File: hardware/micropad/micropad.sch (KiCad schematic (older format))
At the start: 24 parts, among them J1 OLED Connector, J2 Conn_ARM_JTAG_SWD_10, J3 USB_B_Micro, SW1 SW_SPST, SW2 SW_SPST, SW3 SW_SPST, U1 LD1117S33TR_SOT223, U2 STM32F042K6Ux

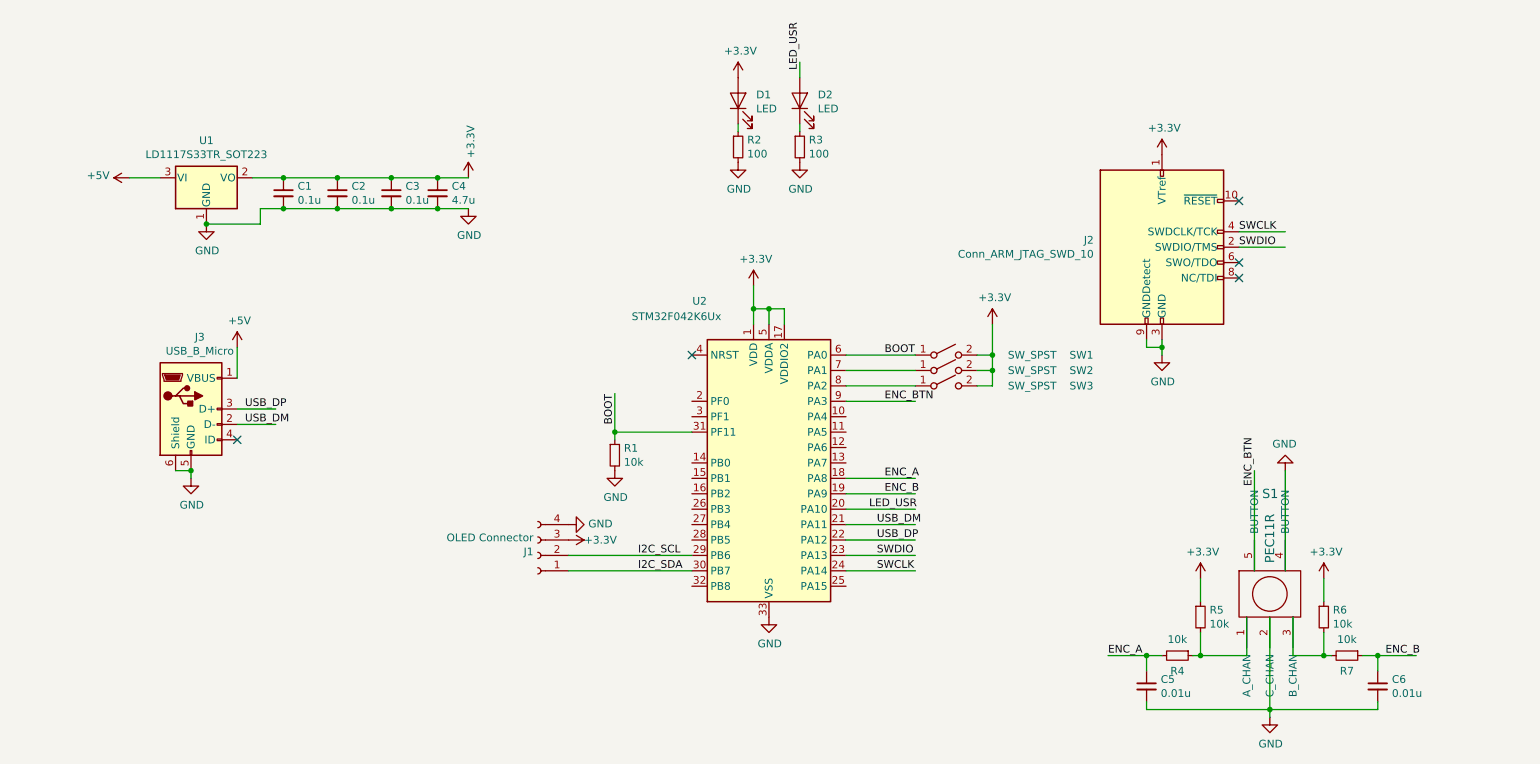
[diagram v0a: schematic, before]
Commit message: Swap in an APA102 instead of the OLED screen
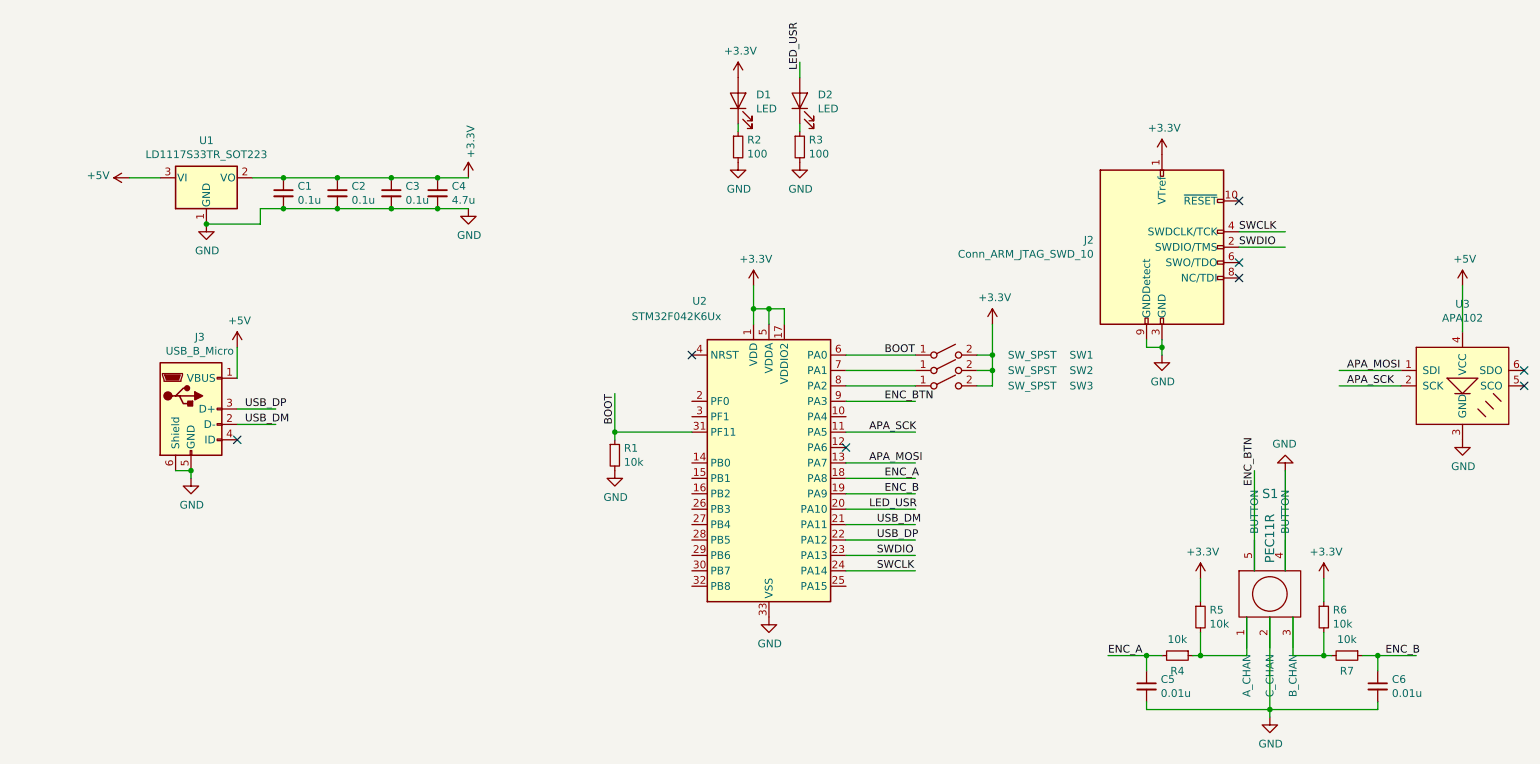
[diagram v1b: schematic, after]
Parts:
- removed J1: OLED Connector, Pin_Headers:Pin_Header_Straight_1x04_Pitch2.54mm, symbol Connector:Conn_01x04_Female
- added U3: APA102, LEDs:LED_RGB_5050-6, symbol apa102:APA102
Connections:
- net labels added: APA_MOSI, APA_SCK
- net labels removed: I2C_SCL, I2C_SDA
- wire segments 79 -> 82
- no-connect marks 5 -> 8
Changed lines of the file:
@@
 Text Label 6350 4550 0    50   ~ 0
 USB_DP
-Text Label 4800 4650 0    50   ~ 0
-I2C_SCL
-Text Label 4800 4750 0    50   ~ 0
-I2C_SDA
 Wire Wire Line
 	2200 3800 2450 3800
@@
 	6150 3550 6600 3550
 $Comp
-L power:+3.3V #PWR08
-U 1 1 5FAF7B5A
-P 4350 4550
-F 0 "#PWR08" H 4350 4400 50  0001 C CNN
-F 1 "+3.3V" V 4350 4650 50  0000 L CNN
-F 2 "" H 4350 4550 50  0001 C CNN
-F 3 "" H 4350 4550 50  0001 C CNN
-	1    4350 4550
-	0    1    1    0
-$EndComp
-$Comp
-L power:GND #PWR07
-U 1 1 5FAF7679
-P 4350 4450
-F 0 "#PWR07" H 4350 4200 50  0001 C CNN
-F 1 "GND" V 4355 4322 50  0000 R CNN
-F 2 "" H 4350 4450 50  0001 C CNN
-F 3 "" H 4350 4450 50  0001 C CNN
-	1    4350 4450
-	0    -1   -1   0
-$EndComp
-$Comp
-L Connector:Conn_01x04_Female J1
-U 1 1 5FAEAC8B
-P 4150 4650
-F 0 "J1" H 4178 4626 50  0000 L CNN
-F 1 "OLED Connector" H 4178 4535 50  0000 L CNN
-F 2 "Pin_Headers:Pin_Header_Straight_1x04_Pitch2.54mm" H 4150 4650 50  0001 C CNN
-F 3 "~" H 4150 4650 50  0001 C CNN
-	1    4150 4650
-	-1   0    0    1
-$EndComp
-Wire Wire Line
-	4350 4650 5150 4650
-Wire Wire Line
-	4350 4750 5150 4750
-$Comp
 L Switch:SW_SPST SW1
 U 1 1 5FAE673E
@@
 Connection ~ 1900 4100
 NoConn ~ 2200 3900
+$Comp
+L apa102:APA102 U3
+U 1 1 5FB655DF
+P 10150 3550
+F 0 "U3" H 10150 4081 50  0000 C CNN
+F 1 "APA102" H 10150 3990 50  0000 C CNN
+F 2 "LEDs:LED_RGB_5050-6" H 10150 3550 50  0001 C CNN
+F 3 "" H 10150 3550 50  0001 C CNN
+	1    10150 3550
+	1    0    0    -1
+$EndComp
+Text Label 9400 3550 0    50   ~ 0
+APA_SCK
+Text Label 9400 3450 0    50   ~ 0
+APA_MOSI
+Wire Wire Line
+	9350 3550 9750 3550
+Wire Wire Line
+	9350 3450 9750 3450
+Wire Wire Line
+	10150 3200 10150 2900
+$Comp
+L power:+5V #PWR07
+U 1 1 5FB8AF8D
+P 10150 2900
+F 0 "#PWR07" H 10150 2750 50  0001 C CNN
+F 1 "+5V" H 10165 3073 50  0000 C CNN
+F 2 "" H 10150 2900 50  0001 C CNN
+F 3 "" H 10150 2900 50  0001 C CNN
+	1    10150 2900
+	1    0    0    -1
+$EndComp
+$Comp
+L power:GND #PWR08
+U 1 1 5FB8B6CE
+P 10150 3900
+F 0 "#PWR08" H 10150 3650 50  0001 C CNN
+F 1 "GND" H 10155 3727 50  0000 C CNN
+F 2 "" H 10150 3900 50  0001 C CNN
+F 3 "" H 10150 3900 50  0001 C CNN
+	1    10150 3900
+	1    0    0    -1
+$EndComp
+NoConn ~ 10550 3450
+NoConn ~ 10550 3550
+Wire Wire Line
+	6150 3850 6600 3850
+Text Label 6300 3850 0    50   ~ 0
+APA_SCK
+Wire Wire Line
+	6150 4050 6600 4050
+Text Label 6300 4050 0    50   ~ 0
+APA_MOSI
+NoConn ~ 6150 3950
 $EndSCHEMATC

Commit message: Use a QFN32 package that's easier to work with
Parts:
- U2: footprint Housings_DFN_QFN:WQFN-32-1EP_5x5mm_Pitch0.5mm -> Housings_DFN_QFN:QFN-32-1EP_5x5mm_Pitch0.5mm
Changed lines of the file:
@@
 F 0 "U2" H 5200 5100 50  0000 C CNN
 F 1 "STM32F042K6Ux" H 5050 5000 50  0000 C CNN
-F 2 "Housings_DFN_QFN:WQFN-32-1EP_5x5mm_Pitch0.5mm" H 5250 3150 50  0001 R CNN
+F 2 "Housings_DFN_QFN:QFN-32-1EP_5x5mm_Pitch0.5mm" H 5250 3150 50  0001 R CNN
 F 3 "http://www.st.com/st-web-ui/static/active/en/resource/technical/document/datasheet/DM00105814.pdf" H 5650 4050 50  0001 C CNN
 	1    5650 4050

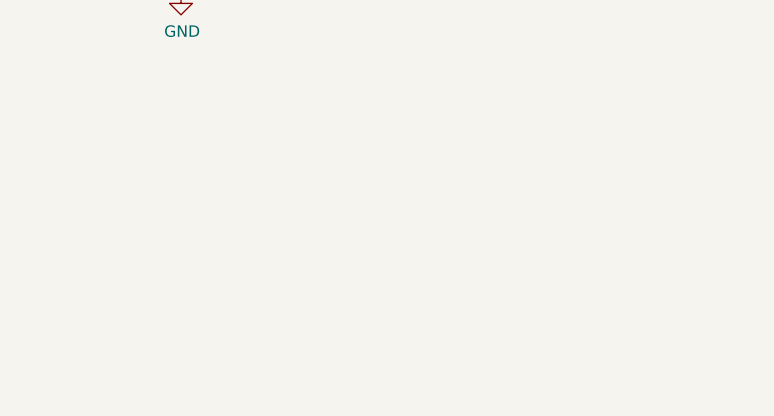
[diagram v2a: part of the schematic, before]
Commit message: Add mounting holes
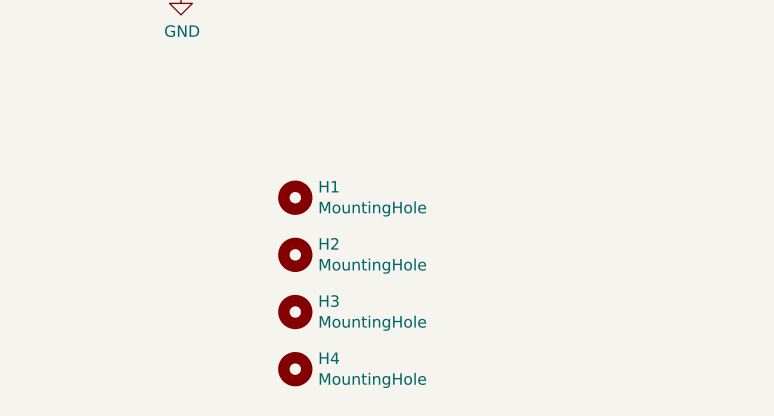
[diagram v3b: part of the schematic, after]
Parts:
- added H1, H2, H3, H4: MountingHole, Mounting_Holes:MountingHole_2.2mm_M2, symbol Mechanical:MountingHole
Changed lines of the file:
@@
 APA_MOSI
 NoConn ~ 6150 3950
+$Comp
+L Mechanical:MountingHole H1
+U 1 1 5FB65D0A
+P 2400 5050
+F 0 "H1" H 2500 5096 50  0000 L CNN
+F 1 "MountingHole" H 2500 5005 50  0000 L CNN
+F 2 "Mounting_Holes:MountingHole_2.2mm_M2" H 2400 5050 50  0001 C CNN
+F 3 "~" H 2400 5050 50  0001 C CNN
+	1    2400 5050
+	1    0    0    -1
+$EndComp
+$Comp
+L Mechanical:MountingHole H2
+U 1 1 5FB66F3B
+P 2400 5300
+F 0 "H2" H 2500 5346 50  0000 L CNN
+F 1 "MountingHole" H 2500 5255 50  0000 L CNN
+F 2 "Mounting_Holes:MountingHole_2.2mm_M2" H 2400 5300 50  0001 C CNN
+F 3 "~" H 2400 5300 50  0001 C CNN
+	1    2400 5300
+	1    0    0    -1
+$EndComp
+$Comp
+L Mechanical:MountingHole H3
+U 1 1 5FB67520
+P 2400 5550
+F 0 "H3" H 2500 5596 50  0000 L CNN
+F 1 "MountingHole" H 2500 5505 50  0000 L CNN
+F 2 "Mounting_Holes:MountingHole_2.2mm_M2" H 2400 5550 50  0001 C CNN
+F 3 "~" H 2400 5550 50  0001 C CNN
+	1    2400 5550
+	1    0    0    -1
+$EndComp
+$Comp
+L Mechanical:MountingHole H4
+U 1 1 5FB67D38
+P 2400 5800
+F 0 "H4" H 2500 5846 50  0000 L CNN
+F 1 "MountingHole" H 2500 5755 50  0000 L CNN
+F 2 "Mounting_Holes:MountingHole_2.2mm_M2" H 2400 5800 50  0001 C CNN
+F 3 "~" H 2400 5800 50  0001 C CNN
+	1    2400 5800
+	1    0    0    -1
+$EndComp
 $EndSCHEMATC

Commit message: Route remaining tracks
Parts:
- U1: footprint TO_SOT_Packages_SMD:SOT-223-3_TabPin2 -> TO_SOT_Packages_SMD:SOT-223
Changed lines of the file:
@@
 F 0 "U1" H 2000 2442 50  0000 C CNN
 F 1 "LD1117S33TR_SOT223" H 2000 2351 50  0000 C CNN
-F 2 "TO_SOT_Packages_SMD:SOT-223-3_TabPin2" H 2000 2400 50  0001 C CNN
+F 2 "TO_SOT_Packages_SMD:SOT-223" H 2000 2400 50  0001 C CNN
 F 3 "http://www.st.com/st-web-ui/static/active/en/resource/technical/document/datasheet/CD00000544.pdf" H 2100 1950 50  0001 C CNN
 	1    2000 2200

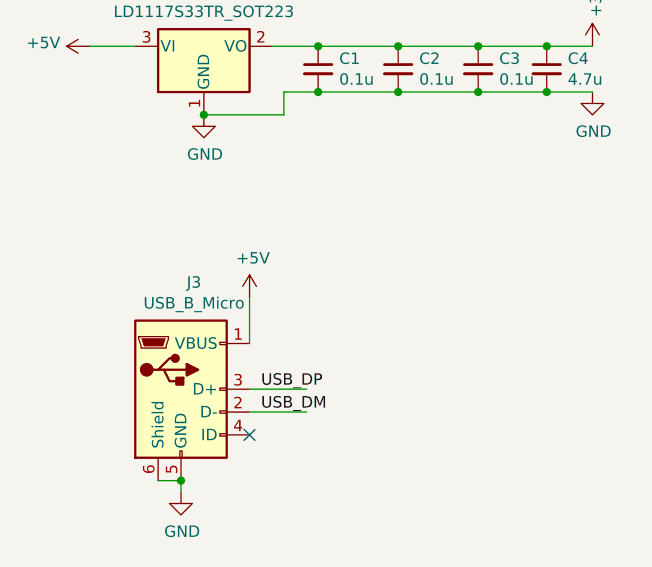
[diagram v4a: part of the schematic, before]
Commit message: Add fuse, fixup DRC and labels
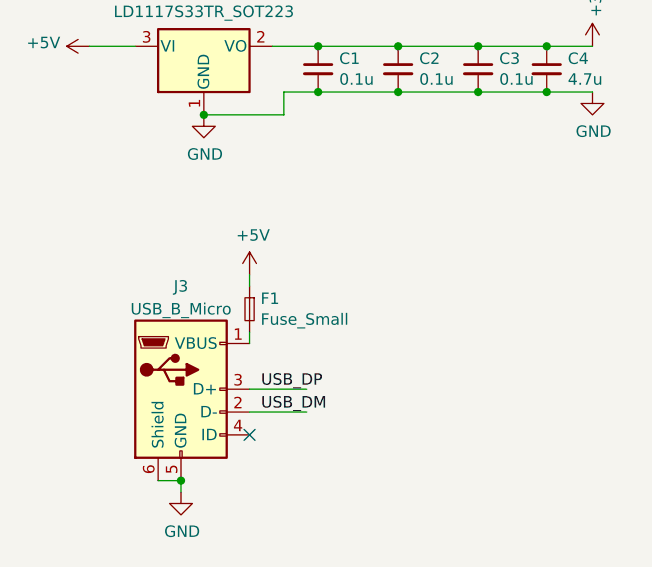
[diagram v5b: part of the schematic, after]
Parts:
- added F1: Fuse_Small, Capacitors_SMD:C_0603, symbol Device:Fuse_Small
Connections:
- wire segments 82 -> 83
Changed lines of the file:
@@
 	1    0    0    -1
 $EndComp
-Wire Wire Line
-	2200 3500 2200 3300
 $Comp
 L power:+5V #PWR04
 U 1 1 5FB029A9
-P 2200 3300
-F 0 "#PWR04" H 2200 3150 50  0001 C CNN
-F 1 "+5V" H 2215 3473 50  0000 C CNN
-F 2 "" H 2200 3300 50  0001 C CNN
-F 3 "" H 2200 3300 50  0001 C CNN
-	1    2200 3300
+P 2200 3200
+F 0 "#PWR04" H 2200 3050 50  0001 C CNN
+F 1 "+5V" H 2215 3373 50  0000 C CNN
+F 2 "" H 2200 3200 50  0001 C CNN
+F 3 "" H 2200 3200 50  0001 C CNN
+	1    2200 3200
 	1    0    0    -1
 $EndComp
@@
 Wire Wire Line
 	4650 3600 4650 3850
-$Comp
-L Connector:USB_B_Micro J3
-U 1 1 5FC27EEA
-P 1900 3700
-F 0 "J3" H 1957 4167 50  0000 C CNN
-F 1 "USB_B_Micro" H 1957 4076 50  0000 C CNN
-F 2 "micropad:XKB-U254_USB" H 2050 3650 50  0001 C CNN
-F 3 "~" H 2050 3650 50  0001 C CNN
-	1    1900 3700
-	1    0    0    -1
-$EndComp
 Wire Wire Line
 	1900 4100 1900 4150
 Wire Wire Line
 	1800 4100 1900 4100
-Connection ~ 1900 4100
 NoConn ~ 2200 3900
 $Comp
@@
 	1    0    0    -1
 $EndComp
+$Comp
+L Device:Fuse_Small F1
+U 1 1 5FB7A019
+P 2200 3350
+F 0 "F1" V 2154 3398 50  0000 L CNN
+F 1 "Fuse_Small" V 2245 3398 50  0000 L CNN
+F 2 "Capacitors_SMD:C_0603" H 2200 3350 50  0001 C CNN
+F 3 "~" H 2200 3350 50  0001 C CNN
+	1    2200 3350
+	0    1    1    0
+$EndComp
+Connection ~ 1900 4100
+$Comp
+L Connector:USB_B_Micro J3
+U 1 1 5FC27EEA
+P 1900 3700
+F 0 "J3" H 1900 4150 50  0000 C CNN
+F 1 "USB_B_Micro" H 1900 4050 50  0000 C CNN
+F 2 "micropad:XKB-U254_USB" H 2050 3650 50  0001 C CNN
+F 3 "~" H 2050 3650 50  0001 C CNN
+	1    1900 3700
+	1    0    0    -1
+$EndComp
+Wire Wire Line
+	2200 3500 2200 3450
+Wire Wire Line
+	2200 3250 2200 3200
 $EndSCHEMATC

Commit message: Update to plated mounting holes
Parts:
- H1, H2, H3, H4: footprint Mounting_Holes:MountingHole_2.2mm_M2 -> Mounting_Holes:MountingHole_2.2mm_M2_ISO7380_Pad
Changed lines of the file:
@@
 F 0 "H1" H 2500 5096 50  0000 L CNN
 F 1 "MountingHole" H 2500 5005 50  0000 L CNN
-F 2 "Mounting_Holes:MountingHole_2.2mm_M2" H 2400 5050 50  0001 C CNN
+F 2 "Mounting_Holes:MountingHole_2.2mm_M2_ISO7380_Pad" H 2400 5050 50  0001 C CNN
 F 3 "~" H 2400 5050 50  0001 C CNN
 	1    2400 5050
@@
 F 0 "H2" H 2500 5346 50  0000 L CNN
 F 1 "MountingHole" H 2500 5255 50  0000 L CNN
-F 2 "Mounting_Holes:MountingHole_2.2mm_M2" H 2400 5300 50  0001 C CNN
+F 2 "Mounting_Holes:MountingHole_2.2mm_M2_ISO7380_Pad" H 2400 5300 50  0001 C CNN
 F 3 "~" H 2400 5300 50  0001 C CNN
 	1    2400 5300
@@
 F 0 "H3" H 2500 5596 50  0000 L CNN
 F 1 "MountingHole" H 2500 5505 50  0000 L CNN
-F 2 "Mounting_Holes:MountingHole_2.2mm_M2" H 2400 5550 50  0001 C CNN
+F 2 "Mounting_Holes:MountingHole_2.2mm_M2_ISO7380_Pad" H 2400 5550 50  0001 C CNN
 F 3 "~" H 2400 5550 50  0001 C CNN
 	1    2400 5550
@@
 F 0 "H4" H 2500 5846 50  0000 L CNN
 F 1 "MountingHole" H 2500 5755 50  0000 L CNN
-F 2 "Mounting_Holes:MountingHole_2.2mm_M2" H 2400 5800 50  0001 C CNN
+F 2 "Mounting_Holes:MountingHole_2.2mm_M2_ISO7380_Pad" H 2400 5800 50  0001 C CNN
 F 3 "~" H 2400 5800 50  0001 C CNN
 	1    2400 5800
